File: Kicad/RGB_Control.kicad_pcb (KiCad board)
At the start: 2 copper layers, 64 x 45 mm, 25 parts, among them J1 Jack-DC, J2 FITA DE LED, Q1 BC848, Q2 BC848, Q3 BC848, Q4 IRF630, Q5 IRF630, Q6 IRF630, U1 Esp32-Devkit-V1, U2 LM7806

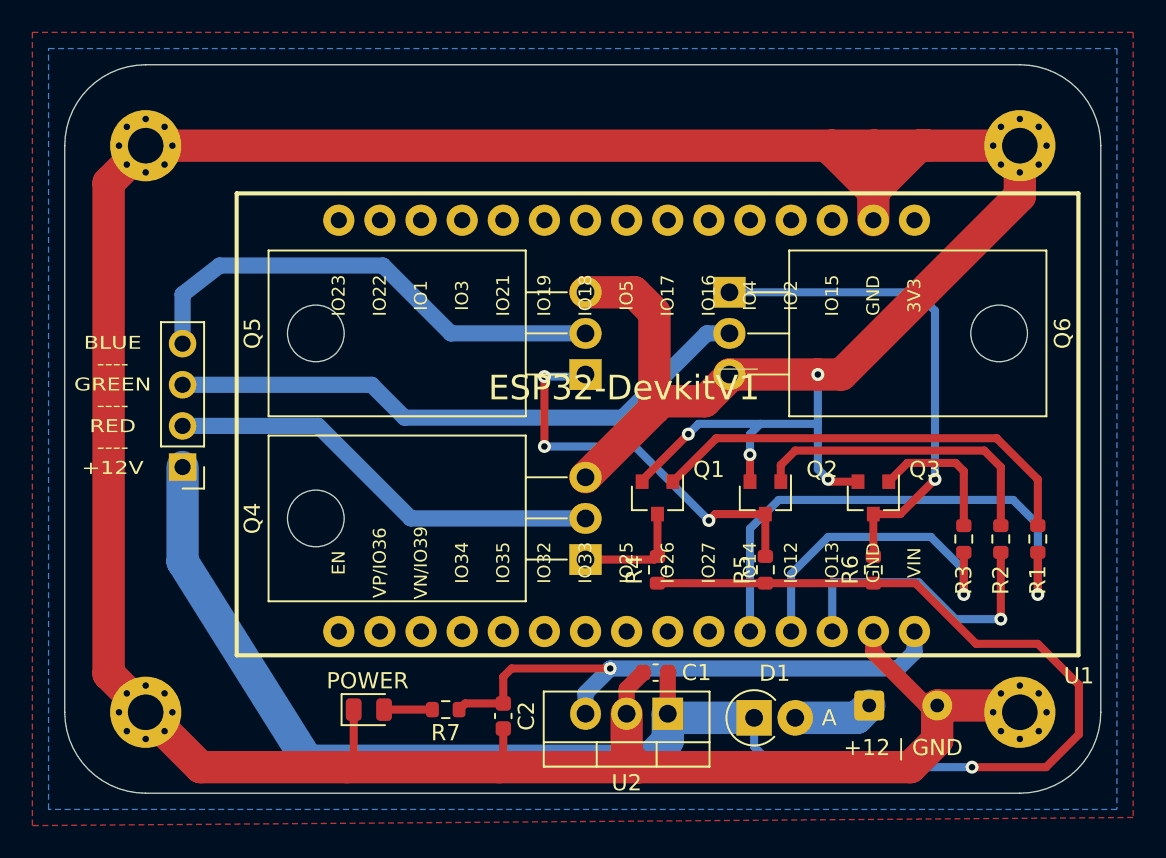
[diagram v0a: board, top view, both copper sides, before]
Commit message: Circuit V2 - BJT
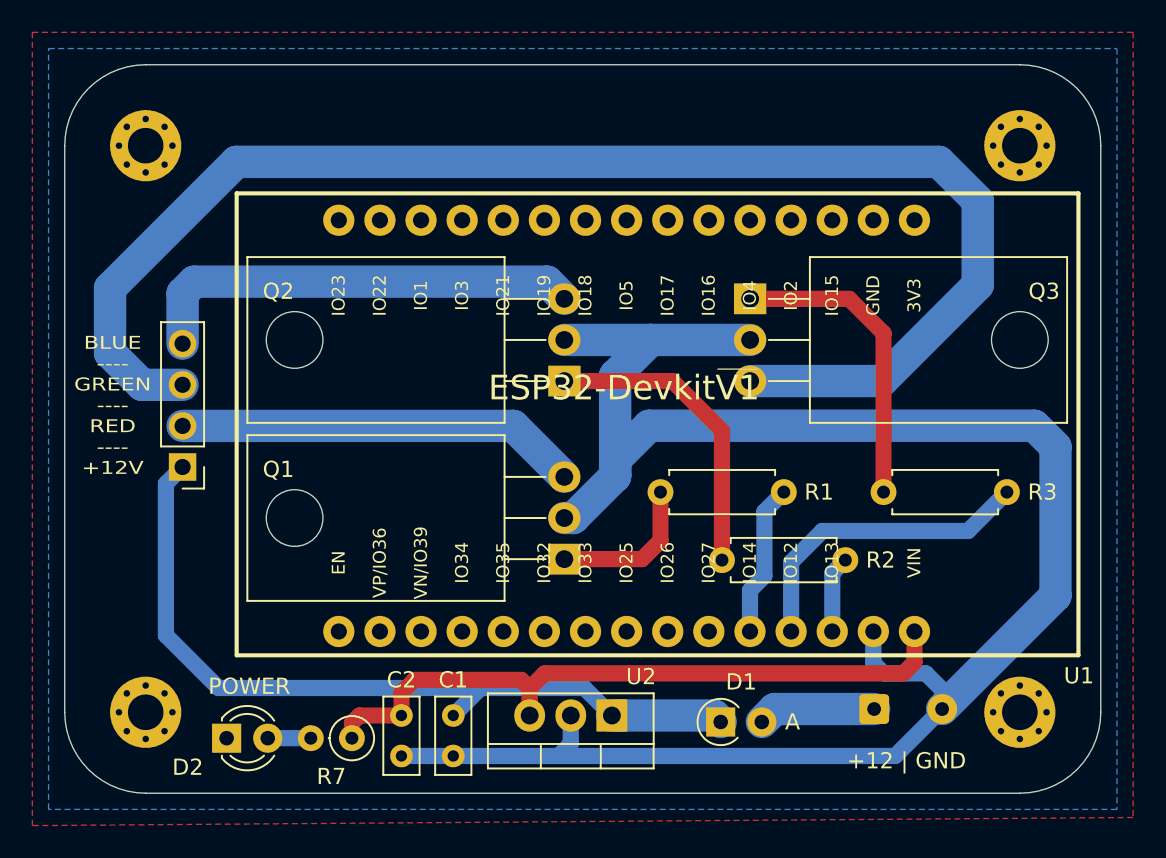
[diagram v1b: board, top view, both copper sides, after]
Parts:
- removed Q4, Q5, Q6: IRF630, Package_TO_SOT_THT:TO-220-3_Horizontal_TabDown
- removed R4, R5, R6: 1k, Resistor_SMD:R_0603_1608Metric
- C1, C2: footprint Capacitor_SMD:C_0603_1608Metric -> Capacitor_THT:C_Rect_L4.6mm_W2.0mm_P2.50mm_MKS02_FKP02
- D1: footprint Diode_THT:D_DO-41_SOD81_P2.54mm_Vertical_AnodeUp -> Diode_THT:D_A-405_P2.54mm_Vertical_AnodeUp
- D2: footprint LED_SMD:LED_0805_2012Metric -> LED_THT:LED_D3.0mm
- Q1, Q2, Q3: value BC848 -> TIP122; footprint Package_TO_SOT_SMD:SOT-23 -> Package_TO_SOT_THT:TO-220-3_Horizontal_TabDown
- R1, R2, R3: footprint Resistor_SMD:R_0603_1608Metric -> Resistor_THT:R_Axial_DIN0207_L6.3mm_D2.5mm_P7.62mm_Horizontal
- R7: footprint Resistor_SMD:R_0603_1608Metric -> Resistor_THT:R_Axial_DIN0207_L6.3mm_D2.5mm_P2.54mm_Vertical
- moved R1 23.5 mm to (94.8, 71.4), turned to 0 degrees
- moved R2 17.3 mm to (98.6, 75.6), turned to 0 degrees
- moved Q3 14.5 mm to (100.3, 59.5)
- moved Q2 14.4 mm to (88.9, 64.5), turned to 90 degrees
- moved C1 12.8 mm to (82.0, 85.2), turned to 270 degrees
- moved D2 8.96 mm to (68.0, 86.6)
- moved Q1 6.89 mm to (88.9, 75.5), turned to 90 degrees
- moved C2 6.29 mm to (78.8, 85.2)
- moved R7 6.06 mm to (75.7, 86.6)
- moved R3 5.74 mm to (108.6, 71.4), turned to 0 degrees
- moved U2 3.45 mm to (91.8, 85.2)
- moved D1 2.08 mm to (98.5, 85.6)
- moved J1 0.37 mm to (108.0, 84.8)
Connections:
- Q1 pad 3: Net-(Q1-Pad3) -> COLOR_RED
- Q2 pad 3: Net-(Q2-Pad3) -> COLOR_BLUE
- Q3 pad 3: Net-(Q3-Pad3) -> COLOR_GREEN
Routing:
- net GND: track 254.6 -> 119.2 mm, vias 4 -> 0
- net +12V: track 107.7 -> 49.7 mm, vias 1 -> 0
- net COLOR_GREEN: track 36.8 -> 88.8 mm
- net Net-(Q3-Pad3): track 30.9 -> 0.00 mm, vias 1 -> 0
- net Net-(Q2-Pad3): track 25.2 -> 0.00 mm, vias 3 -> 0
- net LED_RED: track 32.4 -> 9.48 mm, vias 1 -> 0
- net Net-(Q1-Pad1): track 27.6 -> 9.41 mm
- net LED_BLUE: track 18.5 -> 4.75 mm, vias 1 -> 0
- net Net-(Q3-Pad1): track 8.69 -> 18.9 mm
- net Net-(Q1-Pad3): track 7.14 -> 0.00 mm
- net +6V: track 35.3 -> 42.1 mm, vias 1 -> 0
- net COLOR_BLUE: track 30.3 -> 27.4 mm
- net COLOR_RED: track 27.3 -> 24.9 mm
- net Net-(D1-Pad2): track 4.89 -> 7.27 mm
- net LED_GREEN: track 20.1 -> 19.4 mm, vias 1 -> 0
